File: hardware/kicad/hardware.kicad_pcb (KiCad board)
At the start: 2 copper layers, 33.5 x 34 mm, 11 parts, among them J1 Conn_01x02_Pin, J2 USB_C_Receptacle_USB2.0_14P, U1 STM32L412CBTx, U2 BQ24074RGT, U3 NCP163AFCT330T2G

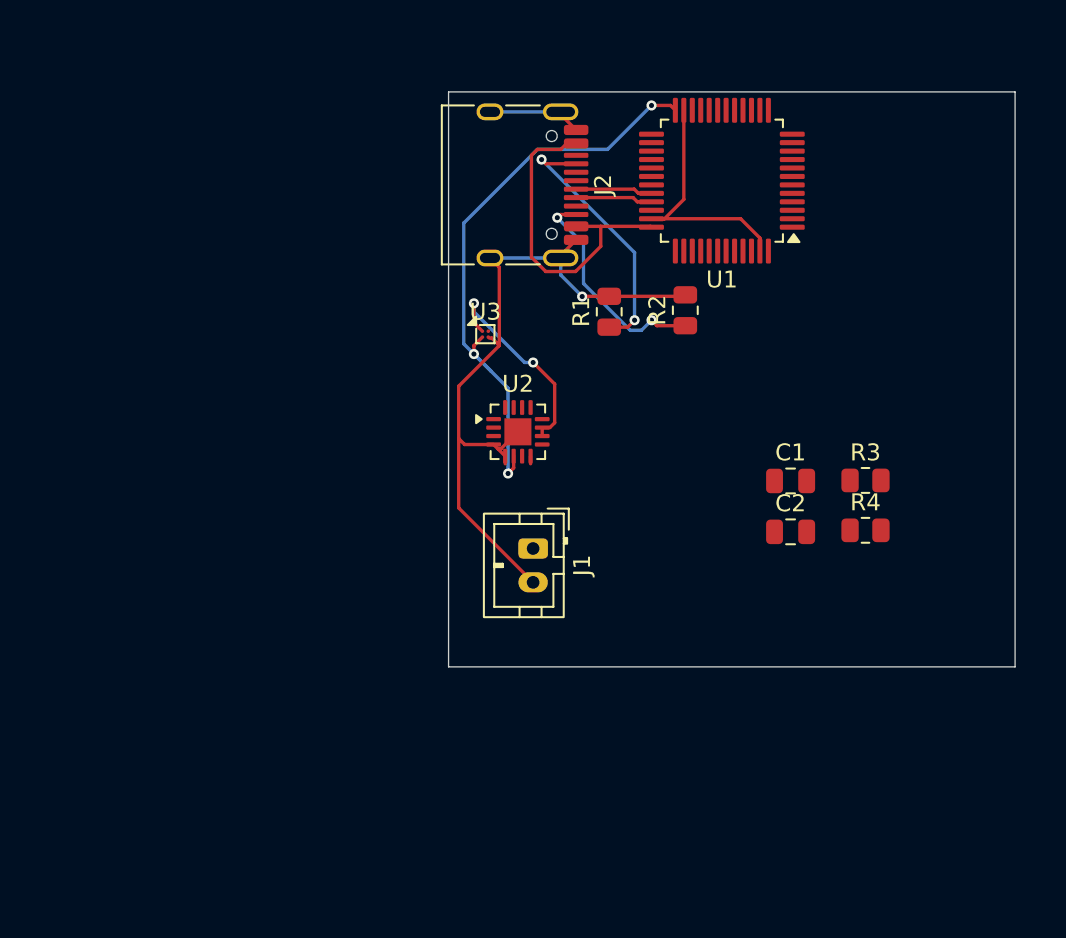
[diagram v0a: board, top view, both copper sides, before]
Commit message: connect gps receiver and add sd card slot
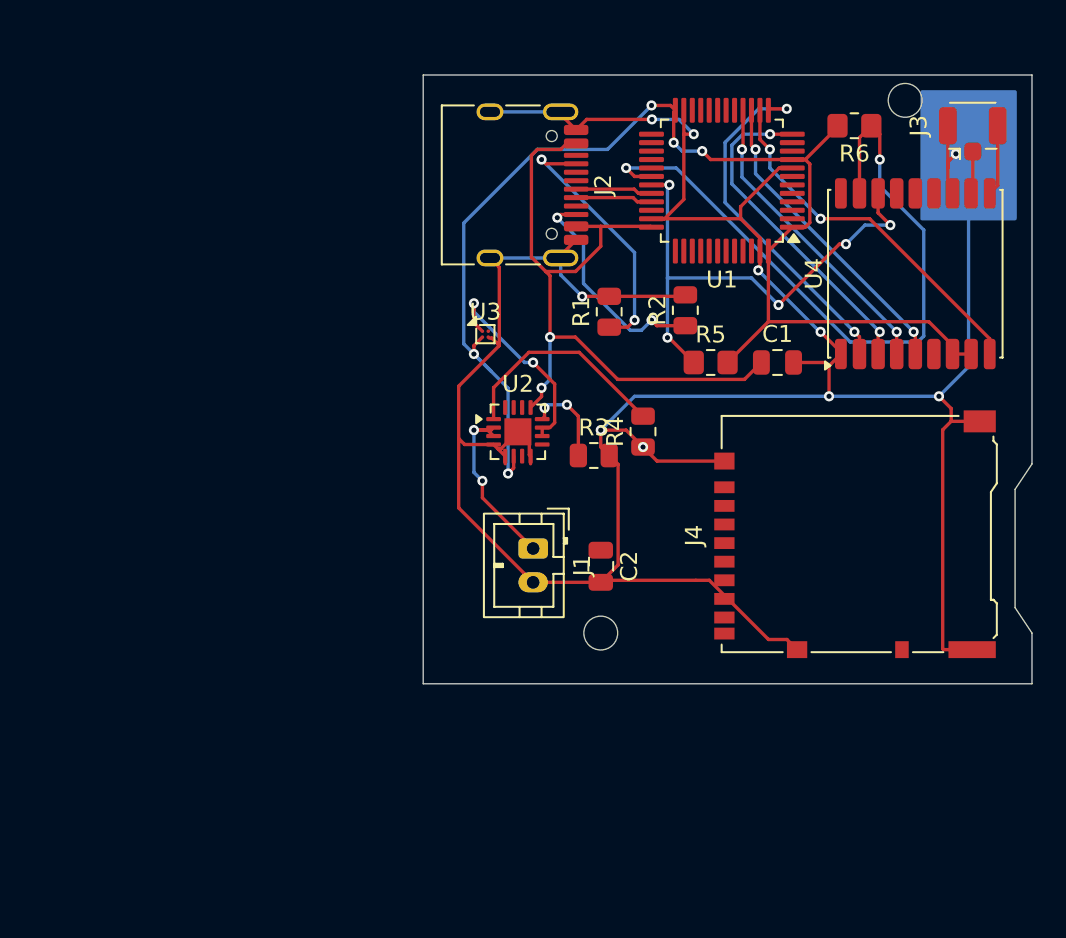
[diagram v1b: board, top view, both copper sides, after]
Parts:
- added J3: Conn_Coaxial, Connector_Coaxial:U.FL_Hirose_U.FL-R-SMT-1_Vertical, F.Cu at (157.5, 85.5)
- added J4: Micro_SD_Card, Connector_Card:microSD_HC_Hirose_DM3AT-SF-PEJM5, F.Cu at (150.5, 109.7)
- added R5: 2.1k, Resistor_SMD:R_0805_2012Metric_Pad1.20x1.40mm_HandSolder, F.Cu at (142.0, 99.5)
- added R6: 2.1k, Resistor_SMD:R_0805_2012Metric_Pad1.20x1.40mm_HandSolder, F.Cu at (150.5, 85.5)
- added U4: MAX-M10S, RF_GPS:ublox_MAX, F.Cu at (154.1, 94.2)
- moved R3 16.1 mm to (135.1, 105.0)
- moved R4 14.4 mm to (138.0, 103.6), turned to 90 degrees
- moved C2 11.4 mm to (135.5, 111.5), turned to -90 degrees
- moved C1 7.05 mm to (145.9, 99.5)
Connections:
- U1 pad 12: unconnected-(U1-PA2-Pad12) -> Net-(U1-PA2)
- U1 pad 13: unconnected-(U1-PA3-Pad13) -> Net-(U1-PA3)
- U1 pad 14: unconnected-(U1-PA4-Pad14) -> Net-(U1-PA4)
- U1 pad 15: unconnected-(U1-PA5-Pad15) -> Net-(U1-PA5)
- U1 pad 16: unconnected-(U1-PA6-Pad16) -> Net-(U1-PA6)
- U1 pad 30: unconnected-(U1-PA9-Pad30) -> Net-(U1-PA9)
- U1 pad 31: unconnected-(U1-PA10-Pad31) -> Net-(U1-PA10)
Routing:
- net GND: track 64.8 -> 191.9 mm, vias 1 -> 10
- net Net-(U1-PA9): track 0.00 -> 41.7 mm, vias 0 -> 2
- net +3.3V: track 35.1 -> 75.7 mm, vias 3 -> 5
- net Net-(U1-PA10): track 0.00 -> 30.3 mm, vias 0 -> 5
- net Net-(U1-VDDUSB): track 19.7 -> 42.3 mm, vias 0 -> 2
- net Net-(U1-PA4): track 0.00 -> 21.7 mm, vias 0 -> 2
- net Net-(U1-PA3): track 0.00 -> 21.4 mm, vias 0 -> 2
- net Net-(U1-PA2): track 0.00 -> 19.9 mm, vias 0 -> 2
- net Net-(U1-PA5): track 0.00 -> 18.4 mm, vias 0 -> 2
- net Net-(U1-PA6): track 0.00 -> 18.2 mm, vias 0 -> 2
- net Net-(U2-TS): track 0.00 -> 13.1 mm
- net Net-(J1-Pin_1): track 0.00 -> 11.0 mm, vias 0 -> 2
- net Net-(U2-ILIM): track 0.00 -> 5.40 mm, vias 0 -> 2
- net Net-(J3-In): track 0.00 -> 2.52 mm
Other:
- board size 33.5 x 34 mm -> 36 x 36 mm

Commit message: reroute main pcb
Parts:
- moved J1 34.4 mm to (109.5, 84.0), turned to 0 degrees
- moved C2 33.3 mm to (110.5, 89.5), turned to 0 degrees
- moved J4 31.1 mm to (122.2, 122.5), turned to 0 degrees
- moved C1 30.1 mm to (116.0, 102.0)
- moved R2 28.4 mm to (113.0, 103.4), turned to -90 degrees
- moved U3 26.1 mm to (110.2, 116.2), turned to 90 degrees
- moved J2 25.3 mm to (106.5, 98.2)
- moved R1 23.3 mm to (113.0, 92.9)
- moved R4 21.7 mm to (117.0, 109.0), turned to 180 degrees
- moved U2 21.6 mm to (110.1, 110.2)
- moved U1 21.3 mm to (123.3, 97.8)
- moved R3 18.1 mm to (117.0, 106.0)
- moved U4 17.6 mm to (137.8, 87.7), turned to 0 degrees
- moved R5 13.7 mm to (147.5, 87.0)
- moved J3 10.1 mm to (149.0, 90.9), turned to 0 degrees
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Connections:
- J4 pad 2: unconnected-(J4-DAT3/CD-Pad2) -> Net-(J4-DAT3/CD)
- J4 pad 3: unconnected-(J4-CMD-Pad3) -> Net-(J4-CMD)
- J4 pad 5: unconnected-(J4-CLK-Pad5) -> Net-(J4-CLK)
- J4 pad 7: unconnected-(J4-DAT0-Pad7) -> Net-(J4-DAT0)
- U1 pad 25: unconnected-(U1-PB12-Pad25) -> Net-(J4-DAT3/CD)
- U1 pad 26: unconnected-(U1-PB13-Pad26) -> Net-(J4-CLK)
- U1 pad 27: unconnected-(U1-PB14-Pad27) -> Net-(J4-DAT0)
- U1 pad 28: unconnected-(U1-PB15-Pad28) -> Net-(J4-CMD)
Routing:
- net +3.3V: track 75.7 -> 100.2 mm, vias 5 -> 2
- net Net-(J4-DAT3/CD): track 0.00 -> 23.7 mm, vias 0 -> 2
- net Net-(J4-DAT0): track 0.00 -> 22.9 mm, vias 0 -> 2
- net Net-(J4-CLK): track 0.00 -> 22.9 mm, vias 0 -> 2
- net Net-(U1-VDDUSB): track 42.3 -> 19.9 mm, vias 2 -> 3
- net Net-(J1-Pin_1): track 11.0 -> 32.5 mm, vias 2 -> 0
- net Net-(J4-CMD): track 0.00 -> 20.7 mm, vias 0 -> 2
- net GND: track 191.9 -> 176.9 mm, vias 10 -> 6
- net Net-(J2-CC1): track 15.6 -> 4.65 mm, vias 2 -> 0
- net Net-(J2-CC2): track 13.3 -> 3.96 mm, vias 2 -> 0
- net Net-(U1-PA9): track 41.7 -> 32.8 mm
- net Net-(U1-PA3): track 21.4 -> 12.6 mm, vias 2 -> 0
- net Net-(U1-PA2): track 19.9 -> 12.3 mm, vias 2 -> 0
- net Net-(U1-PA12): track 4.56 -> 11.4 mm
- net Net-(U1-PA5): track 18.4 -> 12.2 mm
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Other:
- board size 36 x 36 mm -> 49.5 x 50 mm
